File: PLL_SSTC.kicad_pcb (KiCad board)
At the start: 2 copper layers, 96.8 x 99.7 mm, 90 parts, among them J1 Conn_01x01_Socket, J2 Conn_01x01_Socket, J3 Conn_01x01_Socket, J4 Conn_01x01_Socket, J5 Conn_01x02_Socket, J6 Conn_01x02_Socket, J7 Conn_01x02_Socket, Q1 FDS4559, Q2 FDS4559, Q3 IRFP460PBF, Q4 IRFP460PBF, Q5 IRFP460PBF, Q6 IRFP460PBF, SW1 SW_SPST, U1 CD4046BE, U2 74HC74, U3 74HC14N, U4 ATtiny85-20P, U5 74HC08N, U6 MAX809SEUR_T10T, U8 LM7805_TO220

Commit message: fixed power connections and added mounting holes
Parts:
- added C25: 0.1µF, Capacitor_SMD:C_0603_1608Metric_Pad1.08x0.95mm_HandSolder, F.Cu at (211.7, 25.4)
- added REF**: MountingHole_2.7mm_M2.5, MountingHole:MountingHole_2.7mm_M2.5, F.Cu at (172.8, 19.0)
- added REF**: MountingHole_2.7mm_M2.5, MountingHole:MountingHole_2.7mm_M2.5, F.Cu at (263.0, 112.0)
- added REF**: MountingHole_2.7mm_M2.5, MountingHole:MountingHole_2.7mm_M2.5, F.Cu at (203.0, 111.0)
- added REF**: MountingHole_2.7mm_M2.5, MountingHole:MountingHole_2.7mm_M2.5, F.Cu at (263.2, 19.0)
- added Re1: 10k, Resistor_THT:R_Axial_DIN0204_L3.6mm_D1.6mm_P1.90mm_Vertical, F.Cu at (186.5, 33.4)
- moved RV1 3.05 mm to (174.0, 30.0)
- moved D1 2.91 mm to (185.4, 112.6)
- moved J7 2.91 mm to (177.3, 35.7)
- moved U8 2.91 mm to (216.4, 23.9)
- moved +12V1 2.91 mm to (213.8, 28.1)
- moved +12V2 2.91 mm to (218.3, 28.1)
- moved +12V3 2.91 mm to (222.8, 28.1)
- moved C1 2.91 mm to (195.2, 35.3)
- moved C10 2.91 mm to (197.8, 40.3)
- moved C11 2.91 mm to (206.4, 40.3)
- moved C12 2.91 mm to (203.0, 58.3)
- moved C13 2.91 mm to (182.3, 47.4)
- moved C14 2.91 mm to (190.6, 48.2)
- moved C15 2.91 mm to (191.0, 69.5)
- moved C16 2.91 mm to (210.5, 22.9)
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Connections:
- U4 pad 1: unconnected-(U4-~{RESET}/PB5-Pad1) -> Net-(U4-~{RESET}/PB5)
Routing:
- net Net-(U4-~{RESET}/PB5): track 0.00 -> 36.4 mm
- net +300VDC: track 0.17 -> 34.0 mm, vias 0 -> 32
- net GND1: track 9.00 -> 23.1 mm
- net +5V: track 83.8 -> 96.5 mm
- net G3A: track 143.8 -> 148.3 mm
- net Net-(U7-PA): track 8.11 -> 5.39 mm
- net Net-(U1-SIGNAL_IN): track 50.2 -> 52.1 mm
- net Net-(U7-PB): track 47.2 -> 46.5 mm
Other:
- board text added: "1N4148"

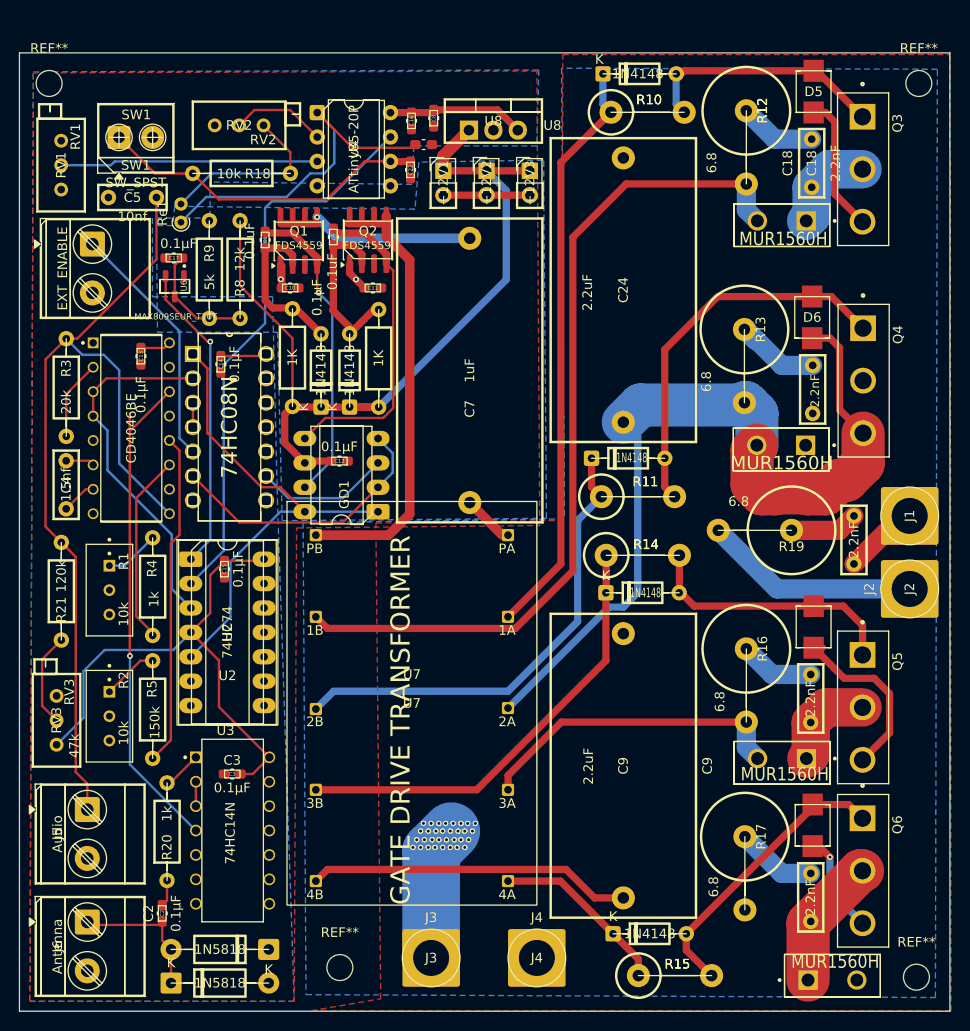
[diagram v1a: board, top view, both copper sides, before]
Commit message: updated drills and attiny file
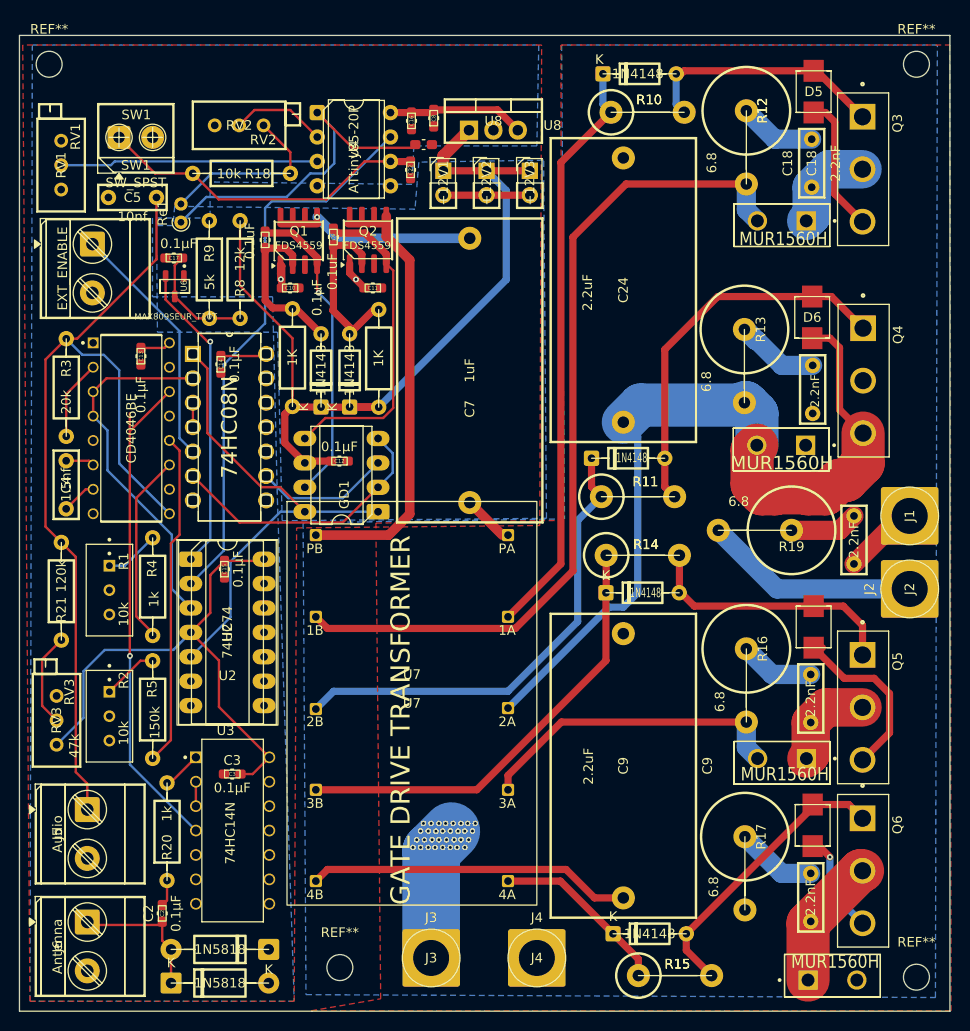
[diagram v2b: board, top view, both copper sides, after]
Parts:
- moved REF** 2.02 mm to (263.0, 17.0)
- moved REF** 2.00 mm to (172.8, 17.0)
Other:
- board size 96.8 x 99.7 mm -> 96.8 x 101.5 mm
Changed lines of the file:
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@@
 			(drillshape 0)
 			(scaleselection 1)
-			(outputdirectory "PCB/")
+			(outputdirectory "Gerbers/")
 		)
 	)
@@
 	(footprint "MountingHole:MountingHole_2.7mm_M2.5"
 		(layer "F.Cu")
-		(at 172.75 19)
+		(at 172.75 17)
 		(descr "Mounting Hole 2.7mm, M2.5, no annular, generated by kicad-footprint-generator mountinghole.py")
 		(tags "mountinghole M2.5")
@@
 	(footprint "MountingHole:MountingHole_2.7mm_M2.5"
 		(layer "F.Cu")
-		(at 263.25 19)
+		(at 263 17)
 		(descr "Mounting Hole 2.7mm, M2.5, no annular, generated by kicad-footprint-generator mountinghole.py")
 		(tags "mountinghole M2.5")
@@
 	)
 	(gr_rect
-		(start 169.66 15.82)
+		(start 169.66 14)
 		(end 266.48 115.54)
 		(stroke
@@
 		(polygon
 			(pts
-				(xy 170.75 114.5) (xy 198.25 114.5) (xy 198.5 65.25) (xy 223.8 65) (xy 223.5 17.7) (xy 171.1 17.9)
+				(xy 170.75 114.5) (xy 198.25 114.5) (xy 198.5 65.25) (xy 223.8 65) (xy 224 15) (xy 170 15)
 			)
 		)
@@
 		(polygon
 			(pts
-				(xy 200 115.5) (xy 207.25 114.25) (xy 206.75 64.75) (xy 226.106122 64.470058) (xy 226.2 16) (xy 266.5 16)
+				(xy 200 115.5) (xy 207.25 114.25) (xy 206.75 64.75) (xy 226.106122 64.470058) (xy 226 15) (xy 266.5 15)
 				(xy 266.6 115.5)
 			)
@@
 		(polygon
 			(pts
-				(xy 223.7 17.6) (xy 223.5 25.5) (xy 210.7 25.5) (xy 210.5 29.5) (xy 189.5 29.25) (xy 189.5 33) (xy 183.5 33)
-				(xy 183.5 41.2) (xy 196 41.2) (xy 196.5 62.25) (xy 198.25 114.5) (xy 170.75 114.5) (xy 171.1 17.8)
+				(xy 223.7 15) (xy 223.5 25.5) (xy 210.7 25.5) (xy 210.5 29.5) (xy 189.5 29.25) (xy 189.5 33) (xy 183.5 33)
+				(xy 183.5 41.2) (xy 196 41.2) (xy 196.5 62.25) (xy 198.25 114.5) (xy 170.75 114.5) (xy 171 15)
 			)
 		)
@@
 		(polygon
 			(pts
-				(xy 199.476155 113.817288) (xy 264.976155 114.117288) (xy 265.176155 17.517288) (xy 226.076155 17.417288)
-				(xy 226.376155 64.317288) (xy 199.176155 64.717288)
+				(xy 199.476155 113.817288) (xy 264.976155 114.117288) (xy 265.176155 15) (xy 226.076155 15) (xy 226.376155 64.317288)
+				(xy 199.176155 64.717288)
 			)
 		)
